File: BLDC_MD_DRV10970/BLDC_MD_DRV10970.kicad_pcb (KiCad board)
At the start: 2 copper layers, 0 parts

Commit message: routed all connections and exported board 3d files
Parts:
- added C1: 0.1uF, Capacitor_SMD:C_0603_1608Metric, F.Cu at (144.0, 102.8)
- added C2: 10uF, Capacitor_SMD:C_0603_1608Metric, F.Cu at (157.7, 104.0)
- added C3: 1000pF, Capacitor_SMD:C_0603_1608Metric, F.Cu at (157.7, 96.4)
- added C4: 1uF, Capacitor_SMD:C_0603_1608Metric, F.Cu at (157.7, 105.6)
- added C5: 2.2uF, Capacitor_SMD:C_0603_1608Metric, F.Cu at (157.7, 102.5)
- added IC1: DRV10970PWP, LibraryLoader:SOP65P640X120-25N, F.Cu at (150.0, 100.0)
- added J1: MIL 02x07, Connector_PinHeader_2.54mm:PinHeader_2x07_P2.54mm_Horizontal, F.Cu at (139.0, 107.5)
- added J2: Conn_01x08_Male, Connector_PinHeader_2.54mm:PinHeader_1x08_P2.54mm_Horizontal, F.Cu at (136.5, 131.0)
- added JP1: SolderJumper_3_Open, Jumper:SolderJumper-3_P2.0mm_Open_TrianglePad1.0x1.5mm, F.Cu at (152.4, 126.1)
- added JP2: SolderJumper_3_Open, Jumper:SolderJumper-3_P2.0mm_Open_TrianglePad1.0x1.5mm, F.Cu at (152.4, 133.1)
- added JP3: SolderJumper_3_Open, Jumper:SolderJumper-3_P2.0mm_Open_TrianglePad1.0x1.5mm, F.Cu at (152.4, 129.5)
- added Q1: BSS138, LibraryLoader:SOT95P240X120-3N, F.Cu at (149.5, 121.6)
- added Q2: BSS138, LibraryLoader:SOT95P240X120-3N, F.Cu at (149.5, 118.0)
- added Q3: BSS138, LibraryLoader:SOT95P240X120-3N, F.Cu at (149.5, 114.4)
- added Q4: BSS138, LibraryLoader:SOT95P240X120-3N, F.Cu at (149.5, 110.8)
- added R1: 10k, Resistor_SMD:R_0603_1608Metric, F.Cu at (146.7, 121.6)
- added R10: 3.3k, Resistor_SMD:R_0603_1608Metric, F.Cu at (155.2, 110.8)
- added R11: 10k, Resistor_SMD:R_0603_1608Metric, F.Cu at (157.7, 99.5)
- added R12: 10k, Resistor_SMD:R_0603_1608Metric, F.Cu at (155.2, 118.0)
- added R13: 20k, Resistor_SMD:R_0603_1608Metric, F.Cu at (157.7, 101.0)
- added R14: 10k, Resistor_SMD:R_0603_1608Metric, F.Cu at (146.7, 94.7)
- added R15: 10k, Resistor_SMD:R_0603_1608Metric, F.Cu at (157.7, 97.9)
- added R2: 10k, Resistor_SMD:R_0603_1608Metric, F.Cu at (146.7, 118.0)
- added R3: 10k, Resistor_SMD:R_0603_1608Metric, F.Cu at (146.7, 114.4)
- added R4: 10k, Resistor_SMD:R_0603_1608Metric, F.Cu at (146.7, 110.8)
- added R5: 10k, Resistor_SMD:R_0603_1608Metric, F.Cu at (152.2, 121.7)
- added R6: 10k, Resistor_SMD:R_0603_1608Metric, F.Cu at (152.2, 118.0)
- added R7: 10k, Resistor_SMD:R_0603_1608Metric, F.Cu at (152.2, 114.4)
- added R8: 10k, Resistor_SMD:R_0603_1608Metric, F.Cu at (152.2, 110.9)
- added R9: 3.3k, Resistor_SMD:R_0603_1608Metric, F.Cu at (155.2, 121.7)
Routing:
- net +5V: track 0.00 -> 71.7 mm, vias 0 -> 5
- net Net-(JP2-Pad2): track 0.00 -> 61.0 mm
- net /FG: track 0.00 -> 45.5 mm
- net Net-(JP3-Pad2): track 0.00 -> 43.5 mm, vias 0 -> 2
- net /FR: track 0.00 -> 40.5 mm
- net Net-(JP1-Pad2): track 0.00 -> 38.9 mm, vias 0 -> 2
- net /COIL_A: track 0.00 -> 38.7 mm
- net +3V3: track 0.00 -> 35.8 mm, vias 0 -> 1
- net /PWM: track 0.00 -> 32.4 mm, vias 0 -> 2
- net VCC: track 0.00 -> 31.2 mm, vias 0 -> 2
- net /RD: track 0.00 -> 26.6 mm, vias 0 -> 2
- net /COIL_B: track 0.00 -> 26.6 mm, vias 0 -> 2
- net /COIL_C: track 0.00 -> 25.6 mm
- net /VCP: track 0.00 -> 24.9 mm, vias 0 -> 2
- net /RD3V3: track 0.00 -> 20.9 mm
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- added copper zone on B.Cu, net GND
- added copper zone on F.Cu, net GND
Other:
- board outline added: 51 x 47.5 mm
- board text added: "0°"
- board text added: "10°"
- board text added: "30°"
- board text added: "5°"
- board text added: "Angle"
- board text added: "BLDC Motor Driver ver 1.0"
- board text added: "BRAKE"
- board text added: "Coasting"
- board text added: "Designed By S. Sanada"
- board text added: "Hall"
- board text added: "Project HARP."

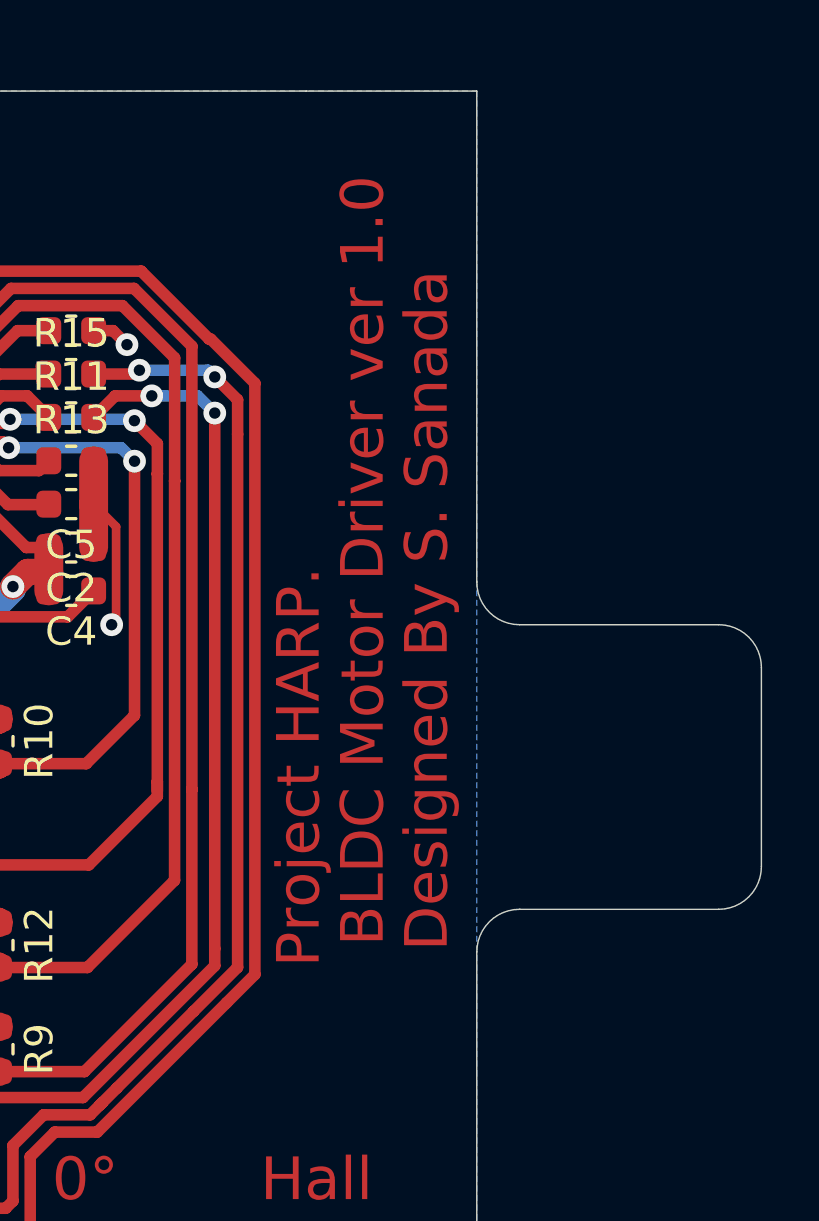
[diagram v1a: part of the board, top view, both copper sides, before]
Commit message: fixed letter mistakes.
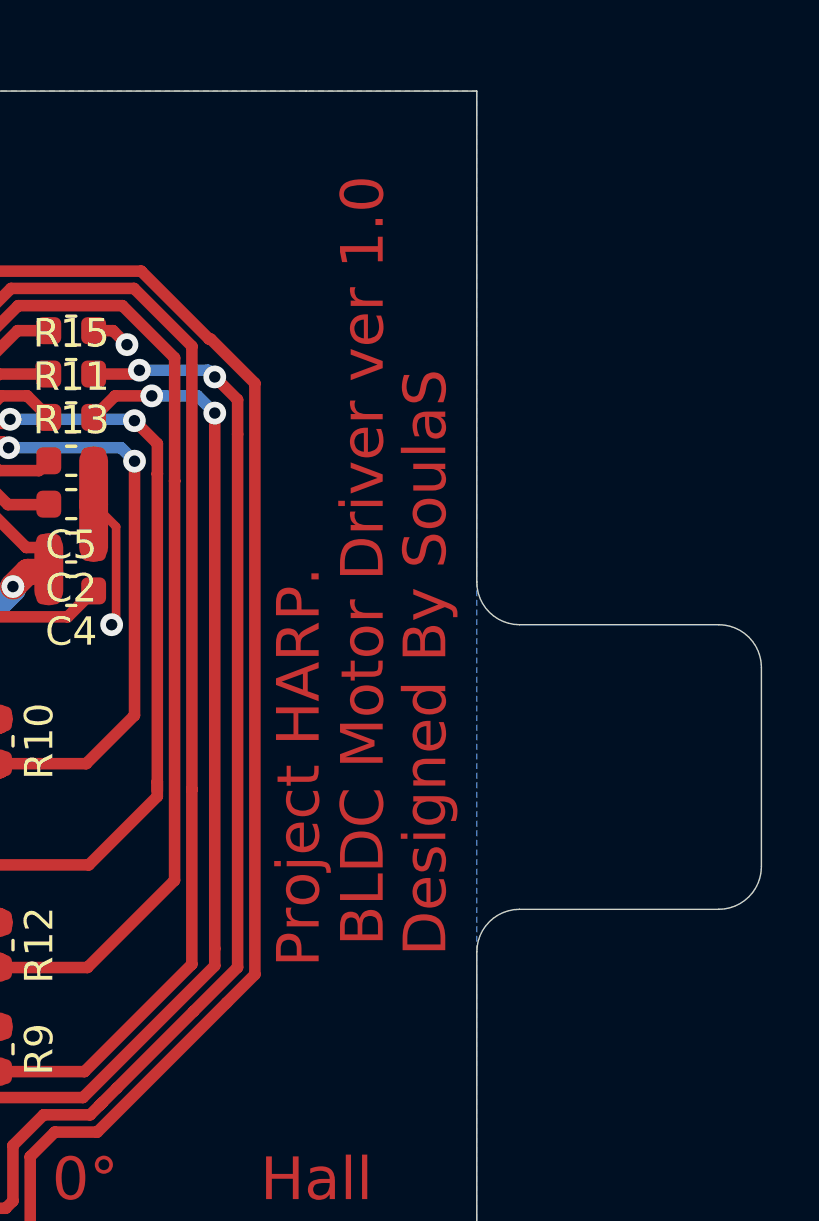
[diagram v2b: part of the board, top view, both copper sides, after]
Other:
- board text added: "Designed By SoulaS"
- board text removed: "Designed By S. Sanada"
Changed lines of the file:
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@@
   (gr_arc (start 180.5 108.25) (end 182 108.25) (angle -90) (layer Edge.Cuts) (width 0.05))
   (gr_arc (start 173.5 105.25) (end 172 105.25) (angle -90) (layer Edge.Cuts) (width 0.05))
-  (gr_text "Designed By S. Sanada" (at 170.25 106.25 90) (layer F.Mask)
+  (gr_text "Designed By SoulaS" (at 170.1992 108.0788 90) (layer F.Mask)
     (effects (font (size 1.5 1.5) (thickness 0.3)))
   )
@@
     (effects (font (size 1.5 1.5) (thickness 0.3)))
   )
-  (gr_text "Designed By S. Sanada" (at 170.25 106.25 90) (layer F.Cu)
+  (gr_text "Designed By SoulaS" (at 170.1992 108.0788 90) (layer F.Cu)
     (effects (font (size 1.5 1.5) (thickness 0.3)))
   )
